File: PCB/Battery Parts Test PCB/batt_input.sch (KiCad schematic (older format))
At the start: 59 parts, among them P1 CONN_9, Q1 MOSFET_P/NDS0605, Q2 MOSFET_P, Q3 MOSFET_P, Q4 MOSFET_N/NDS7002A, Q5 MOSFET_N/NDS7002A, Q6 MOSFET_N/NDS7002A, Q7 MOSFET_N/NDS7002A, Q8 MOSFET_N/NDS7002A

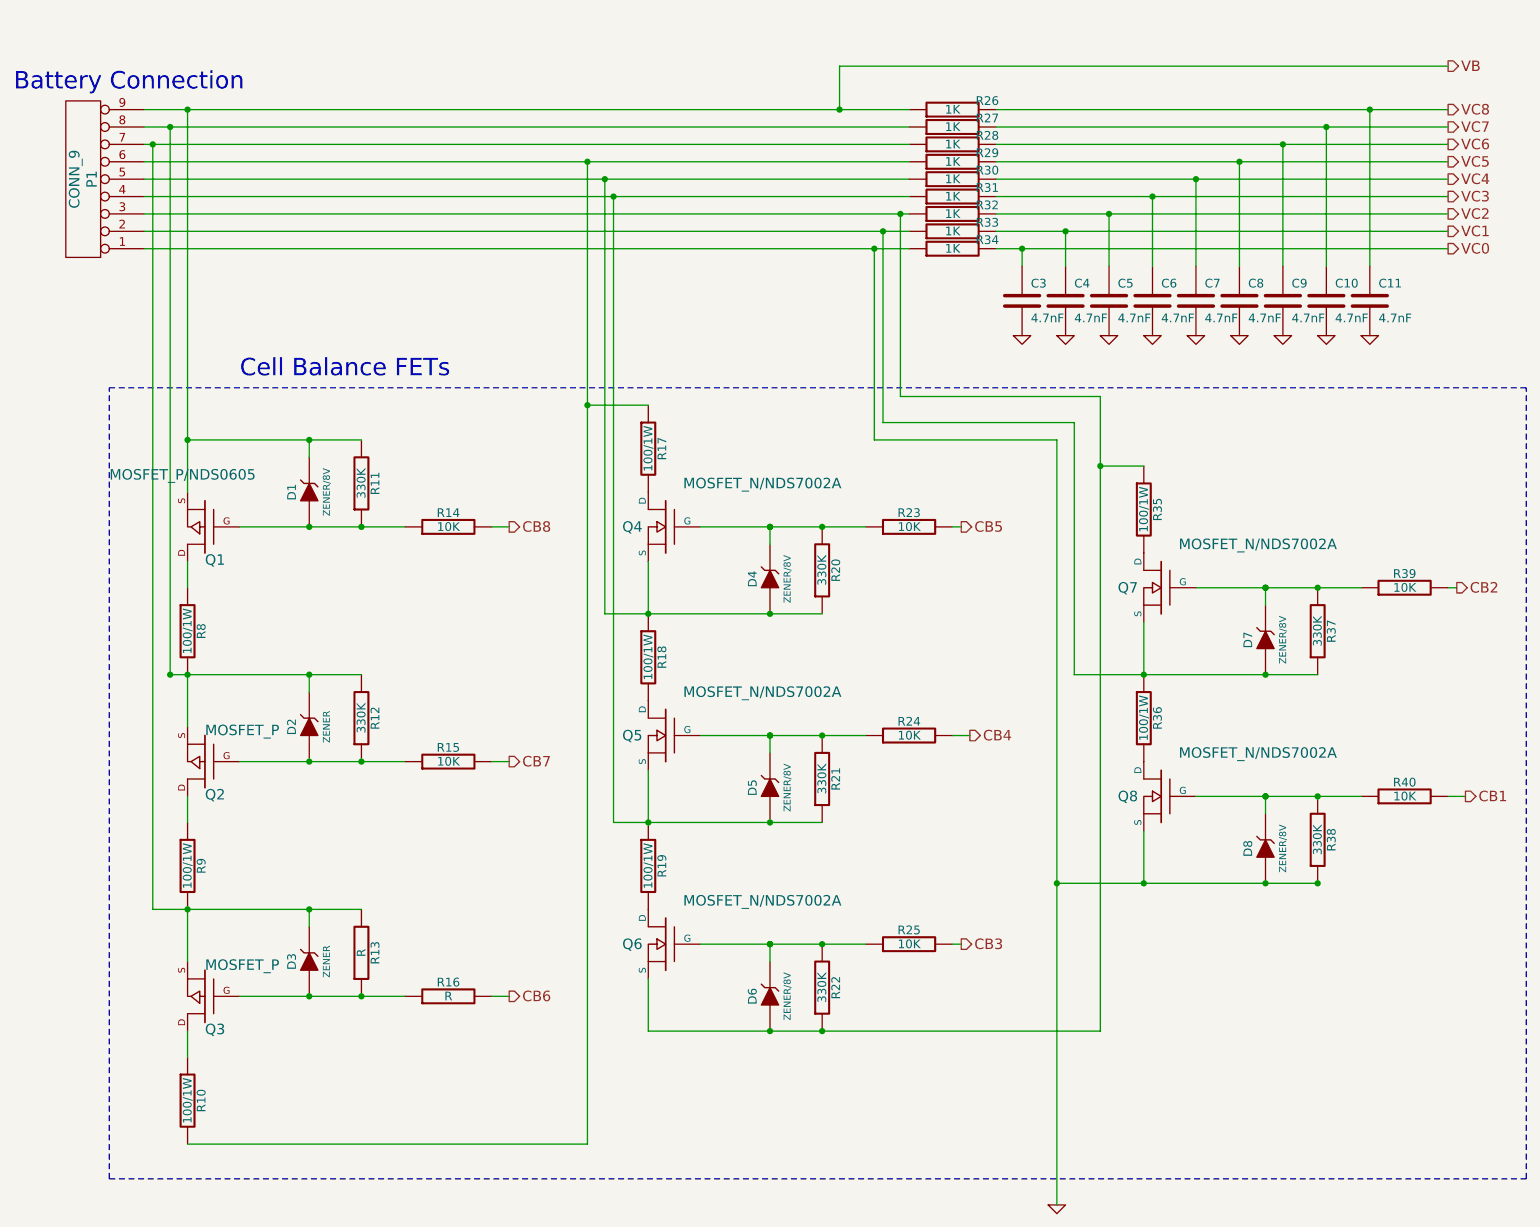
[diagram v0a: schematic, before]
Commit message: finished schematic with new battery monitor
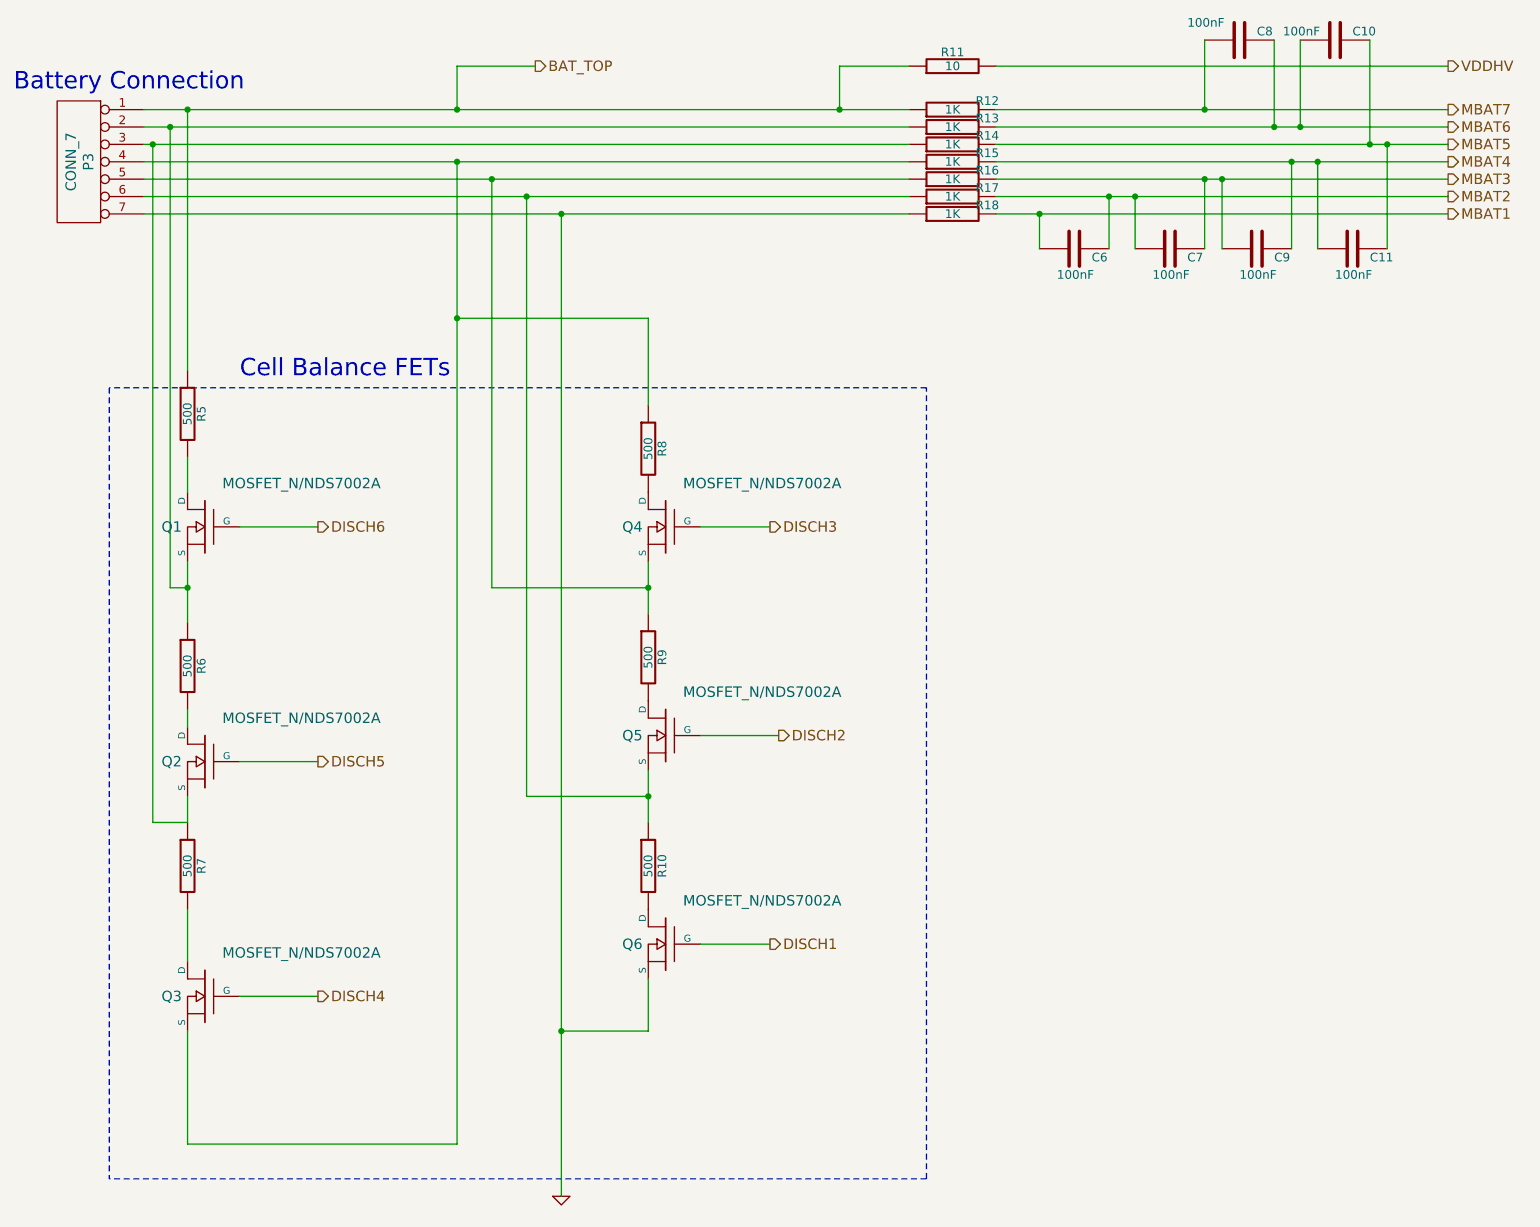
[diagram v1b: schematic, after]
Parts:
- removed C3, C4, C5: 4.7nF, symbol C
- removed D1, D4, D5, D6, D7, D8: ZENER/8V, symbol ZENER
- removed D2, D3: ZENER, symbol ZENER
- removed P1: CONN_9, symbol CONN_9
- removed Q1: MOSFET_P/NDS0605, symbol MOSFET_P
- removed Q2, Q3: MOSFET_P, symbol MOSFET_P
- removed Q7, Q8: MOSFET_N/NDS7002A, symbol MOSFET_N
- removed R12, R20, R21, R22, R37, R38: 330K, symbol R
- removed R13, R16: R, symbol R
- removed R14, R15, R23, R24, R25, R39, R40: 10K, symbol R
- removed R17, R18, R19, R35, R36: 100/1W, symbol R
- removed R33, R34: 1K, symbol R
- added P3: CONN_7, symbol CONN_7
- added Q1, Q2, Q3: MOSFET_N/NDS7002A, symbol MOSFET_N
- added R6, R7, R8: 500, symbol R
- C10, C11, C6, C7, C8, C9: value 4.7nF -> 100nF
- R10, R9: value 100/1W -> 500
- R11: value 330K -> 10
- R5: renamed from R8; value 100/1W -> 500
- renumbered R26 to R12, R27 to R13, R28 to R14, R29 to R15, R30 to R16, R31 to R17, R32 to R18
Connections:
- net GND: now also Q6.S, R18.1, P3.7 (P7); no longer C10.2, C11.2, C6.2, C7.2, C8.2, C9.2
- net at Q4.S, R16.1: now also R9.1, P3.5 (P5)
- net at Q5.S, R17.1: now also R10.1, P3.6 (P6)
- net at R14.1: now also P3.3 (P3), Q2.S, R7.1; no longer R9.2
- net at R15.1: now also P3.4 (P4), Q3.S, R8.1; no longer R10.2
- net at R13.1: now also P3.2 (P2), Q1.S, R6.1; no longer R5.2
- net BAT_TOP: now reaches R11.1
- net BAT_TOP: now also R12.1, R5.1, P3.1 (P1)
- net at Q4.D: now also R8.2
- net DISCH3: now reaches Q4.G
- net at Q5.D: now also R9.2
- net DISCH2: now reaches Q5.G
- net at Q6.D: now also R10.2
- net DISCH1: now reaches Q6.G
- net VB renamed VDDHV
- net VDDHV: no longer R12.1
- net VC2 renamed MBAT1
- net MBAT1: now also C6.2
- net VC3 renamed MBAT2
- net MBAT2: now also C7.2
- net VC4 renamed MBAT3
- net MBAT3: now also C9.2
- net VC5 renamed MBAT4
- net MBAT4: now also C11.2, C9.1; no longer C8.1
- net VC6 renamed MBAT5
- net MBAT5: now also C10.1, C11.1; no longer C9.1
- net VC7 renamed MBAT6
- net MBAT6: now also C10.2, C8.1; no longer C10.1
- net VC8 renamed MBAT7
- net MBAT7: now also C8.2; no longer C11.1
- new net: Q1.D, R5.2
- new net: Q2.D, R6.2
- new net: Q3.D, R7.2
- new net DISCH4: Q3.G
- new net DISCH5: Q2.G
- new net DISCH6: Q1.G
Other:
- moved on the sheet: C6, R5
